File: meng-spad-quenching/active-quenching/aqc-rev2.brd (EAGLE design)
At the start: 120 x 74.9 mm, 297 parts, among them IC1 ADCMP582, IC10 74AHC1G04DBV, IC11 74AHC1G04DBV, IC12 TLV272DGK, IC13 TLV271DBV, IC14 74AHC1G04DBV, IC15 ALD1106, IC16 ALD1107, IC17 74AHC1G04DBV, IC18 LT1534-1, IC19 LT1534-1, IC2 TLV271DBV, IC20 STM32F411RE, IC22 TPS7A3001, IC24 TPS7A4901, IC25 TPS7A4901, IC27 USBLC6-2SC6Y, IC28 MAX572X, IC3 NC7SV74K8X, IC4 TLV272DGK, IC5 NC7WZ16P6X, IC6 LTC1711, IC7 DS1100LU-20+, IC8 LM1117, M1 BSS806N, M2 BSS806N, M3 BSS806N, Q1 IRLML6402TRPBF, Q2 MMBTH81, Q3 MMBTH81, Q5 MMBTH81, Q7 MMBTH81, Q8 MMBTH81, SW1 MCU_RST, T1 MMBTH10, T2 MMBTH10, T5 MMBTH10, T6 MMBTH10, T7 MMBTH10, T8 MMBTH10, T9 MMBTH10, U1 SN65EPT21DGK, U2 SN65EPT22DGK, X1 CONN_SPAD, X2 CONN_PHOTON_COUNTER, X3 KEYSTONE-7774, X4 KEYSTONE-7774, X5 CONN_SMU, X6 CONN_FORCE_QUENCH, X7 CONN_PULLDN_SENSE, X8 PN61729-S

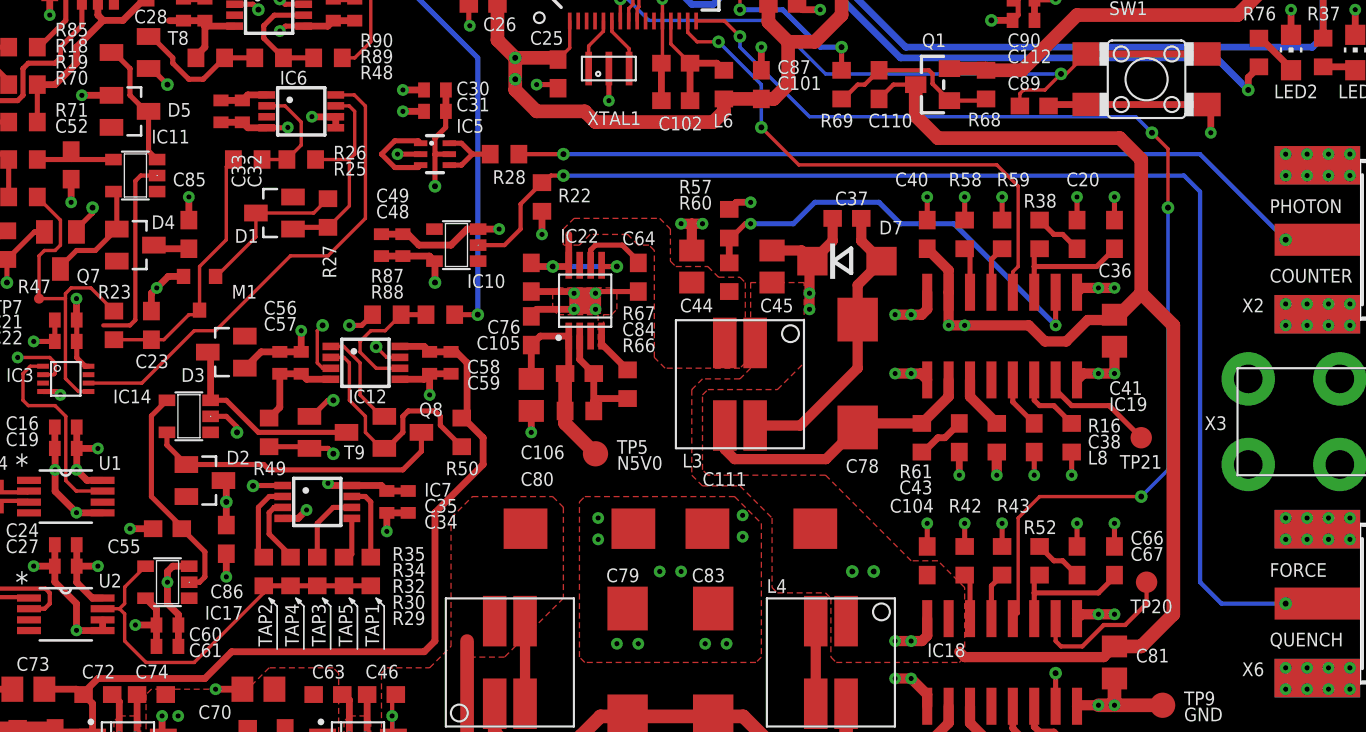
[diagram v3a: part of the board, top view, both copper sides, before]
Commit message: Added ground plane under bottom-side hispeed traces
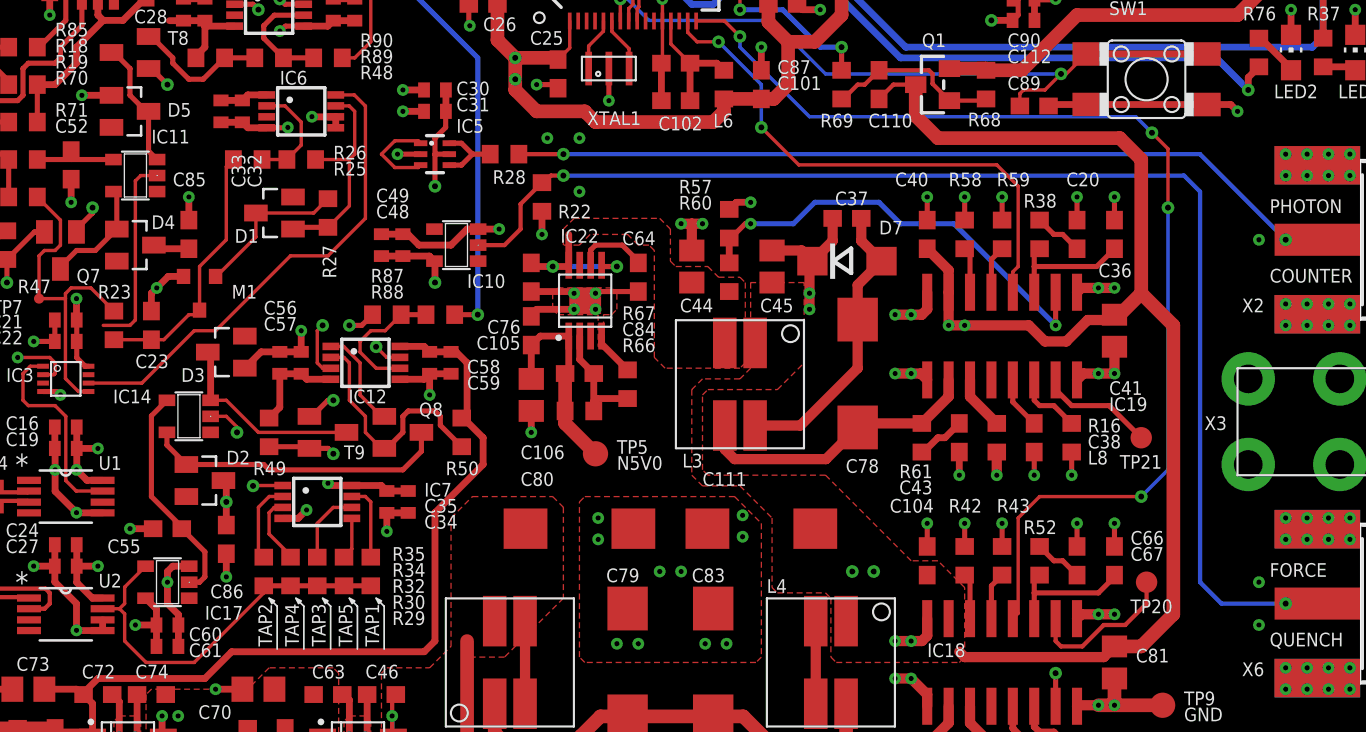
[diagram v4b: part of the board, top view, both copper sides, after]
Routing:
- net GND: track 332.4 -> 332.6 mm, vias 359 -> 365

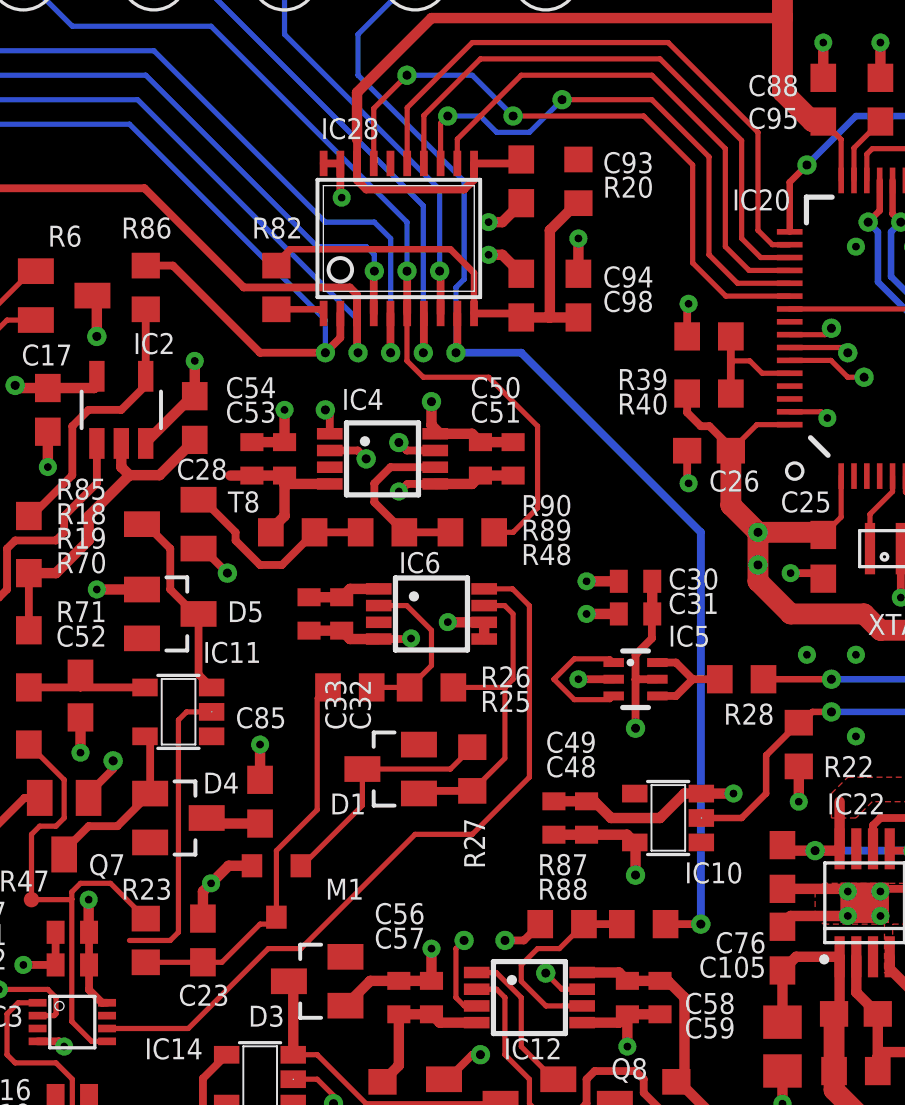
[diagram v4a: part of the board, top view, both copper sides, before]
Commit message: More routing, fixed -5V rail naming issue
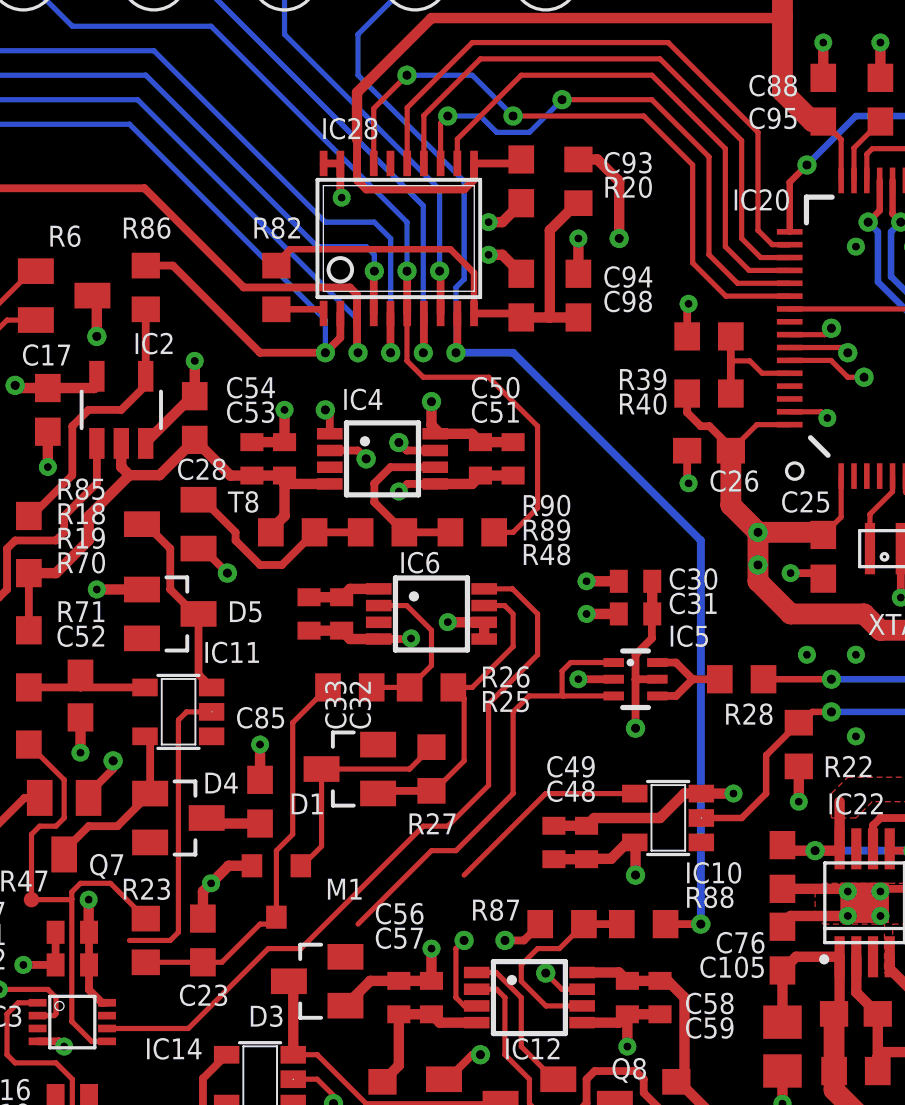
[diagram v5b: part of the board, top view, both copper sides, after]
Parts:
- moved D1 1.59 mm to (52.4, 39.1)
- moved R27 1.59 mm to (55.6, 39.1)
- moved C48 0.95 mm to (61.6, 36.2)
- moved C49 0.95 mm to (60.3, 36.2)
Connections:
- removed net PP_N5V0: C12.1, C13.1, C53.1, C54.1, C56.1, C57.1, IC1.13, IC12.4, IC4.4, R15.1, R48.1, R49.1
- net PP_N5V0_ANALOG: now also C12.1, C13.1, C53.1, C54.1, C56.1, C57.1, IC1.13, IC12.4, IC4.4, R15.1, R48.1, R49.1
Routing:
- net PP_N5V0_ANALOG: track 25.1 -> 48.8 mm
- net PP_N5V0: track 21.7 -> 0.00 mm
- net PP_P5V0_ANALOG: track 191.0 -> 207.5 mm, vias 11 -> 12
- net LOGIC_QUENCH: track 24.8 -> 38.0 mm
- net !FORCE_QUENCH: track 0.00 -> 7.95 mm
- net N$36: track 9.41 -> 8.75 mm
- net ONE_SHOT_CAP: track 15.6 -> 16.2 mm
- net ONE_SHOT_CLR: track 12.9 -> 12.4 mm
